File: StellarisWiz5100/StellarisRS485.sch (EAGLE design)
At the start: 10 parts

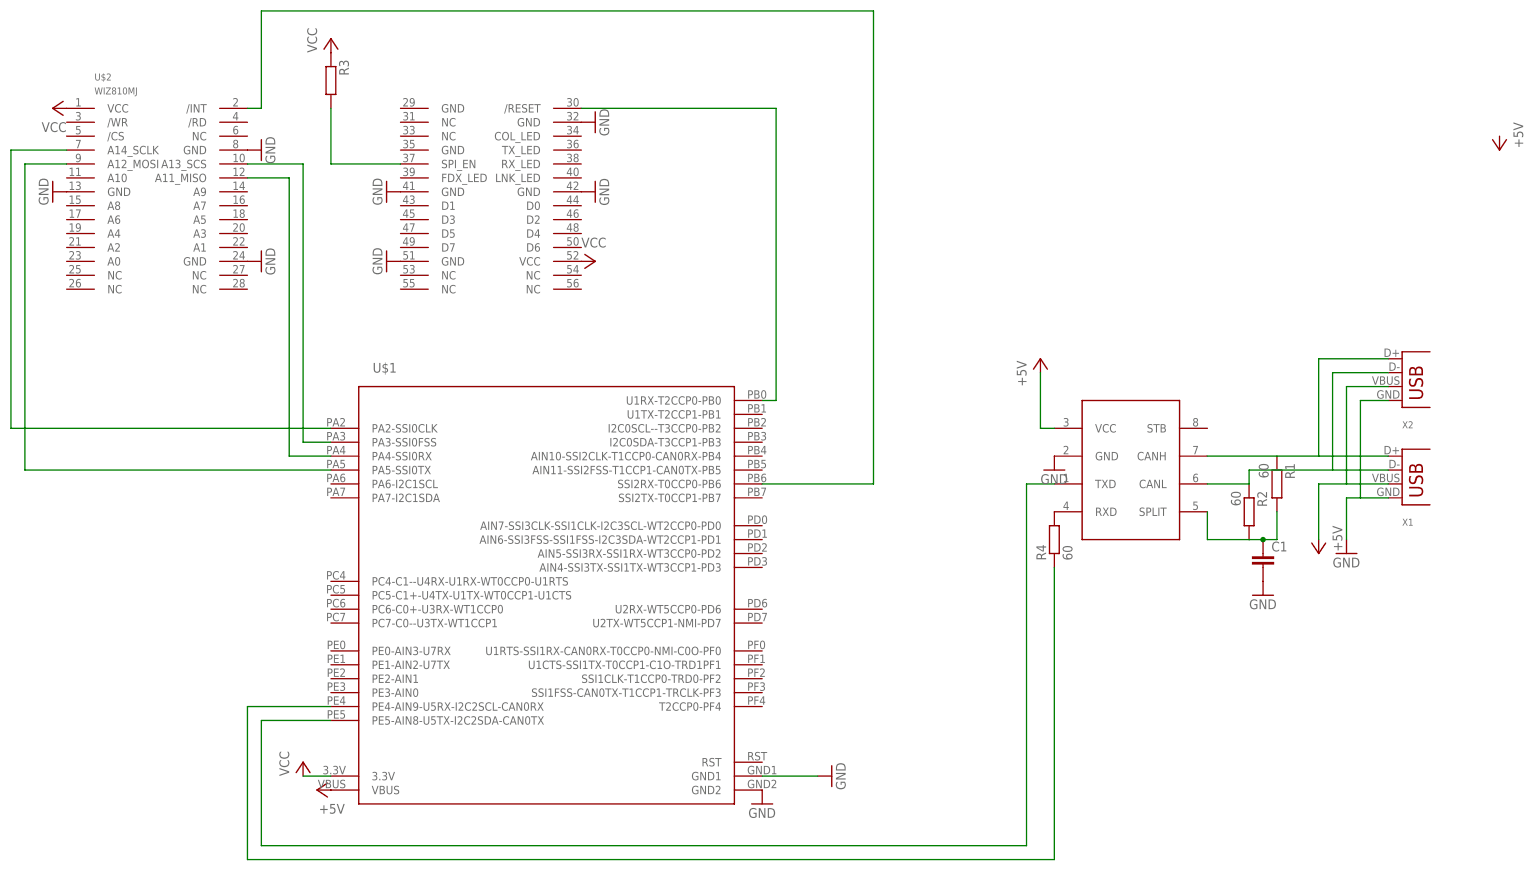
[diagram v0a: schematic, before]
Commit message: 
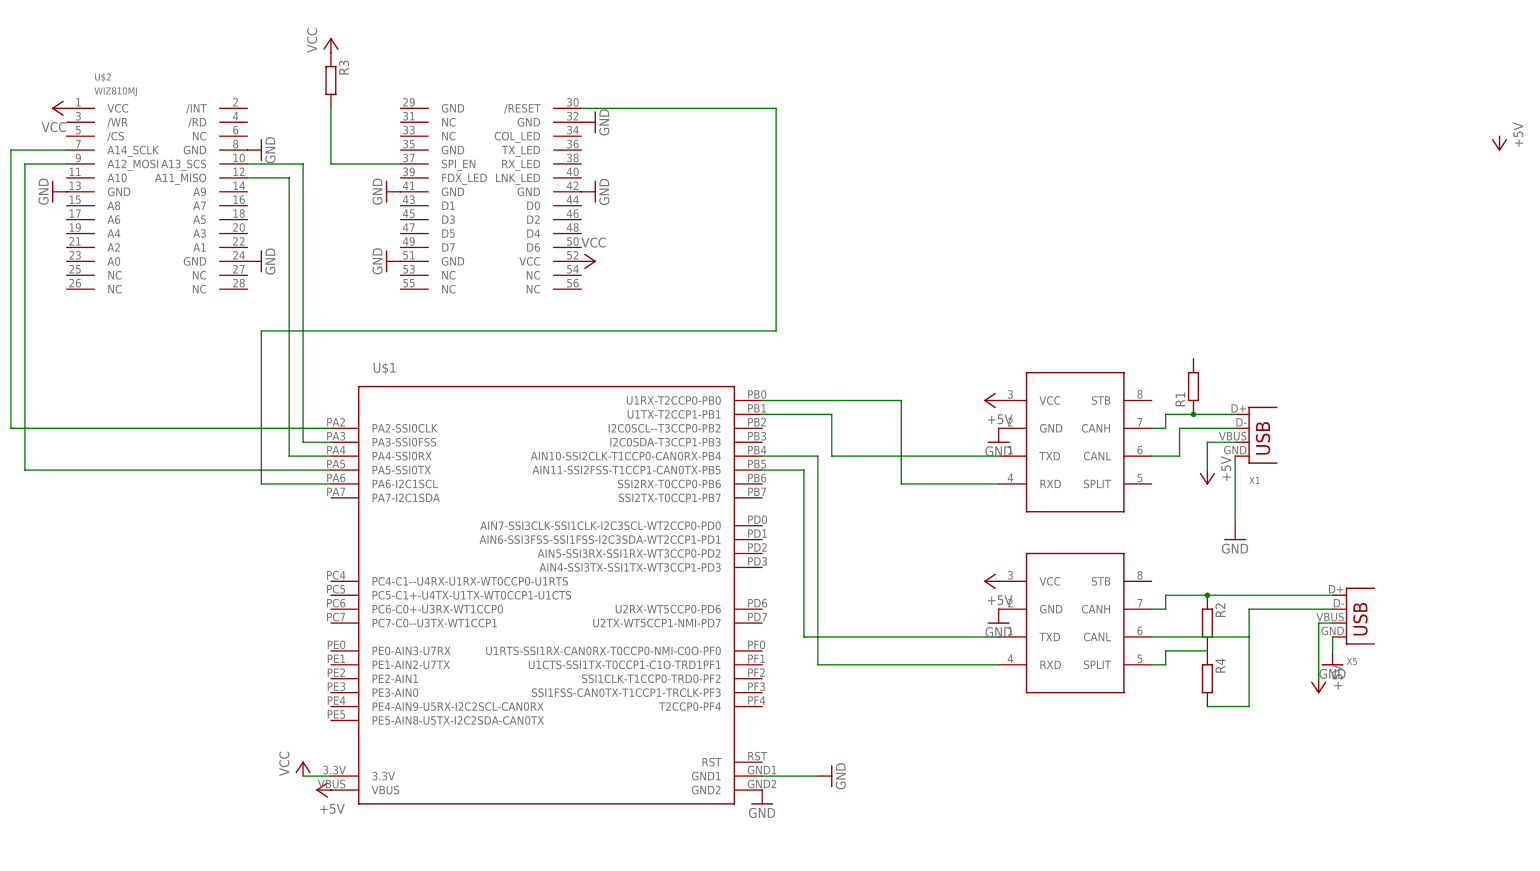
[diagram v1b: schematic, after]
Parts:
- removed C1: (no value), rcl:C-EU025-040X050
- removed X2: (no value), lieven:USB-B-H
- added U$4: TJA1040, lieven:TJA1040
- added X5: (no value), lieven:USB-A-H
- R1, R2, R4: value 60 -> (none)
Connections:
- removed net N$12: R2.1, U$3.CANL, X1.D-, X2.D-
- removed net N$13: U$1.SSI2RX-T0CCP0-PB6, U$2./INT
- new net N$17: U$1.U1RX-T2CCP0-PB0, U$3.RXD
- new net N$18: R4.2, U$4.CANL, X5.D-
- new net N$19: U$1.AIN11-SSI2FSS-T1CCP1-CAN0TX-PB5, U$4.TXD
- new net N$20: U$1.AIN10-SSI2CLK-T1CCP0-CAN0RX-PB4, U$4.RXD
- net +5V: now also U$4.VCC, X5.VBUS; no longer X2.VBUS
- net GND: now also U$4.GND, X5.GND; no longer C1.2, X2.GND
- net N$1: now also U$1.PA6-I2C1SCL; no longer U$1.U1RX-T2CCP0-PB0
- net N$11: now also R4.1, U$4.SPLIT; no longer C1.1, R1.2, U$3.SPLIT
- net N$2: now also R1.1, U$3.CANH, X1.D+; no longer R4.2, U$3.RXD
- net N$4: now also U$3.CANL, X1.D-; no longer R4.1, U$1.PE4-AIN9-U5RX-I2C2SCL-CAN0RX
- net N$5: now also R2.1, U$4.CANH, X5.D+; no longer R1.1, U$3.CANH, X1.D+, X2.D+
- net N$7: now also U$1.U1TX-T2CCP1-PB1; no longer U$1.PE5-AIN8-U5TX-I2C2SDA-CAN0TX
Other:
- moved on the sheet: R1, R2, R4, X1
